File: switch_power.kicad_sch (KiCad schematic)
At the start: 32 parts

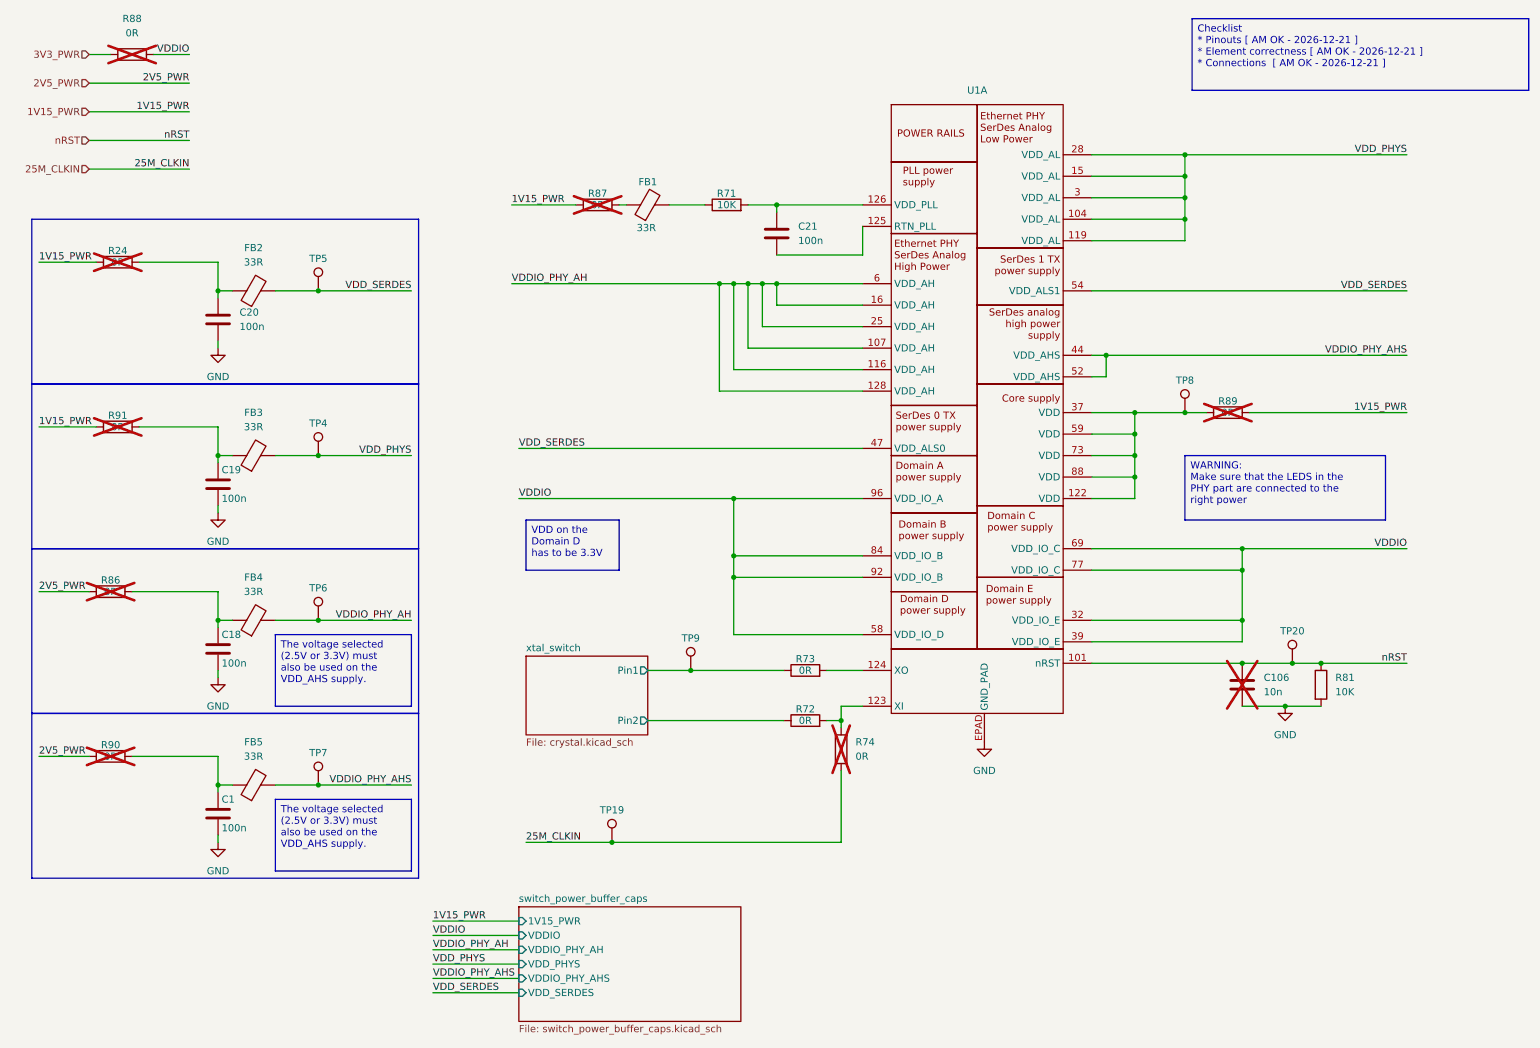
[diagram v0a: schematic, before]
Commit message: removes 25M CLK input for switch. Refs: #1
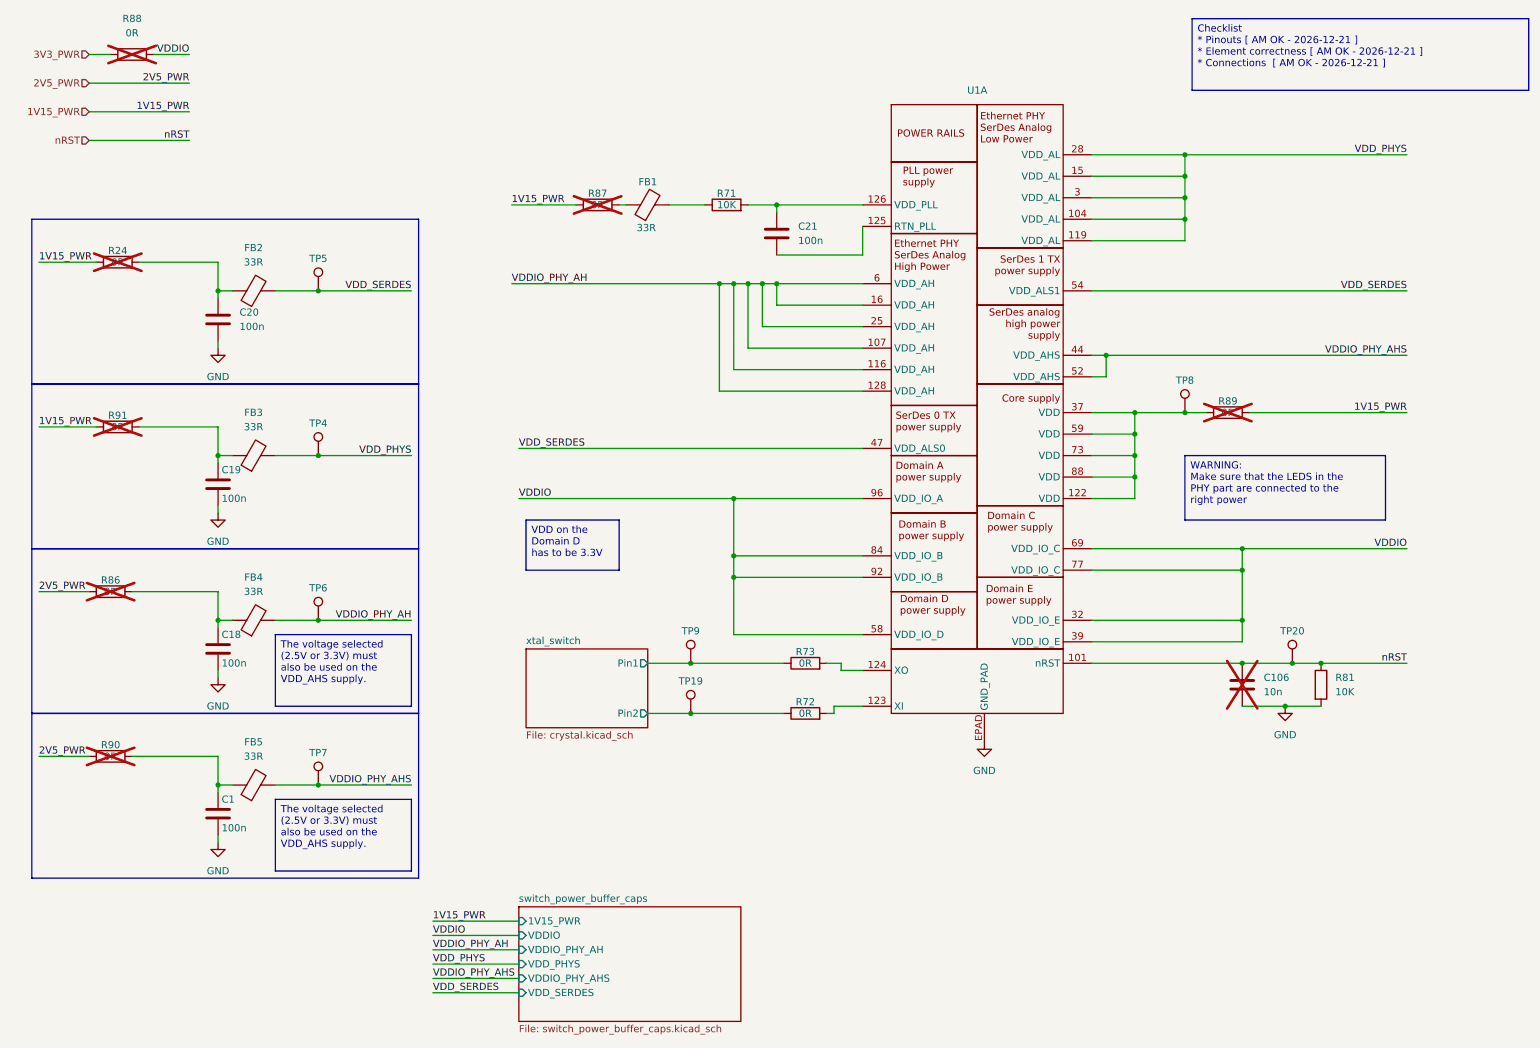
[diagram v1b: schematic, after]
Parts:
- removed R74: 0R, KL_Footprints:R_0603, symbol KL_R:R_0R_100mW_5_0603
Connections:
- net 25M_CLKIN is gone; now on net xtal_switch/Pin2: TP19.1
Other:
- moved on the sheet: R72, R73, TP9

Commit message: adds footprint for ferrite bead. Refs: #1
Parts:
- FB1, FB2, FB3, FB4, FB5: footprint (none) -> KL_Footprints:BLM18P; Digikey 490-5220-2-ND;490-5220-1-ND;490-5220-6-ND -> 490-5220-1-ND; Mouser 81-BLM18PG330SN1D -> 81-BLM18PG330SN1D
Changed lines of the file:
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@@
 			)
 		)
-		(property "Footprint" ""
-			(at 57.15 146.05 0)
+		(property "Footprint" "KL_Footprints:BLM18P"
+			(at 64.008 133.858 0)
 			(effects
 				(font
@@
 			)
 		)
-		(property "Datasheet" ""
-			(at 57.15 146.05 0)
+		(property "Datasheet" "https://pim.murata.com/asset/pim4/ferriteBeadInductortypefilter/ENFA0003_PDF_FERRITEBEADINDUCTORTYPEFILTER?lastModifiedDatetime=20250707190934"
+			(at 57.912 129.286 0)
 			(effects
 				(font
@@
 			)
 		)
-		(property "Mouser" " 81-BLM18PG330SN1D"
+		(property "Mouser" "81-BLM18PG330SN1D"
 			(at 39.37 147.574 0)
 			(effects
@@
 			)
 		)
-		(property "Digikey" "490-5220-2-ND;490-5220-1-ND;490-5220-6-ND"
+		(property "Digikey" "490-5220-1-ND"
 			(at 43.434 140.97 0)
 			(effects
@@
 			)
 		)
-		(property "Footprint" ""
-			(at 57.15 87.63 0)
+		(property "Footprint" "KL_Footprints:BLM18P"
+			(at 64.008 75.438 0)
 			(effects
 				(font
@@
 			)
 		)
-		(property "Datasheet" ""
-			(at 57.15 87.63 0)
+		(property "Datasheet" "https://pim.murata.com/asset/pim4/ferriteBeadInductortypefilter/ENFA0003_PDF_FERRITEBEADINDUCTORTYPEFILTER?lastModifiedDatetime=20250707190934"
+			(at 57.912 70.866 0)
 			(effects
 				(font
@@
 			)
 		)
-		(property "Mouser" " 81-BLM18PG330SN1D"
+		(property "Mouser" "81-BLM18PG330SN1D"
 			(at 39.37 89.154 0)
 			(effects
@@
 			)
 		)
-		(property "Digikey" "490-5220-2-ND;490-5220-1-ND;490-5220-6-ND"
+		(property "Digikey" "490-5220-1-ND"
 			(at 43.434 82.55 0)
 			(effects
@@
 			)
 		)
-		(property "Footprint" ""
-			(at 127 43.18 0)
+		(property "Footprint" "KL_Footprints:BLM18P"
+			(at 133.858 30.988 0)
 			(effects
 				(font
@@
 			)
 		)
-		(property "Datasheet" ""
-			(at 127 43.18 0)
+		(property "Datasheet" "https://pim.murata.com/asset/pim4/ferriteBeadInductortypefilter/ENFA0003_PDF_FERRITEBEADINDUCTORTYPEFILTER?lastModifiedDatetime=20250707190934"
+			(at 127.762 26.416 0)
 			(effects
 				(font
@@
 			)
 		)
-		(property "Mouser" " 81-BLM18PG330SN1D"
+		(property "Mouser" "81-BLM18PG330SN1D"
 			(at 109.22 44.704 0)
 			(effects
@@
 			)
 		)
-		(property "Digikey" "490-5220-2-ND;490-5220-1-ND;490-5220-6-ND"
+		(property "Digikey" "490-5220-1-ND"
 			(at 113.284 38.1 0)
 			(effects
@@
 			)
 		)
-		(property "Footprint" ""
-			(at 57.15 116.84 0)
+		(property "Footprint" "KL_Footprints:BLM18P"
+			(at 64.008 104.648 0)
 			(effects
 				(font
@@
 			)
 		)
-		(property "Datasheet" ""
-			(at 57.15 116.84 0)
+		(property "Datasheet" "https://pim.murata.com/asset/pim4/ferriteBeadInductortypefilter/ENFA0003_PDF_FERRITEBEADINDUCTORTYPEFILTER?lastModifiedDatetime=20250707190934"
+			(at 57.912 100.076 0)
 			(effects
 				(font
@@
 			)
 		)
-		(property "Mouser" " 81-BLM18PG330SN1D"
+		(property "Mouser" "81-BLM18PG330SN1D"
 			(at 39.37 118.364 0)
 			(effects
@@
 			)
 		)
-		(property "Digikey" "490-5220-2-ND;490-5220-1-ND;490-5220-6-ND"
+		(property "Digikey" "490-5220-1-ND"
 			(at 43.434 111.76 0)
 			(effects
@@
 			)
 		)
-		(property "Footprint" ""
-			(at 57.15 58.42 0)
+		(property "Footprint" "KL_Footprints:BLM18P"
+			(at 64.008 46.228 0)
 			(effects
 				(font
@@
 			)
 		)
-		(property "Datasheet" ""
-			(at 57.15 58.42 0)
+		(property "Datasheet" "https://pim.murata.com/asset/pim4/ferriteBeadInductortypefilter/ENFA0003_PDF_FERRITEBEADINDUCTORTYPEFILTER?lastModifiedDatetime=20250707190934"
+			(at 57.912 41.656 0)
 			(effects
 				(font
@@
 			)
 		)
-		(property "Mouser" " 81-BLM18PG330SN1D"
+		(property "Mouser" "81-BLM18PG330SN1D"
 			(at 39.37 59.944 0)
 			(effects
@@
 			)
 		)
-		(property "Digikey" "490-5220-2-ND;490-5220-1-ND;490-5220-6-ND"
+		(property "Digikey" "490-5220-1-ND"
 			(at 43.434 53.34 0)
 			(effects

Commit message: updates component details for ordering. Refs: #1
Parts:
- TP19, TP20, TP4, TP5, TP6, TP7, TP8, TP9: now left out of the parts list
- U1: value ~ -> LAN96455F-I/8MW; Digikey (none) -> 150-LAN96455F-I/8MW-ND; Mouser (none) -> 579-LAN96455FI8MW; manf# LAN96455F-I/8MW -> (none)

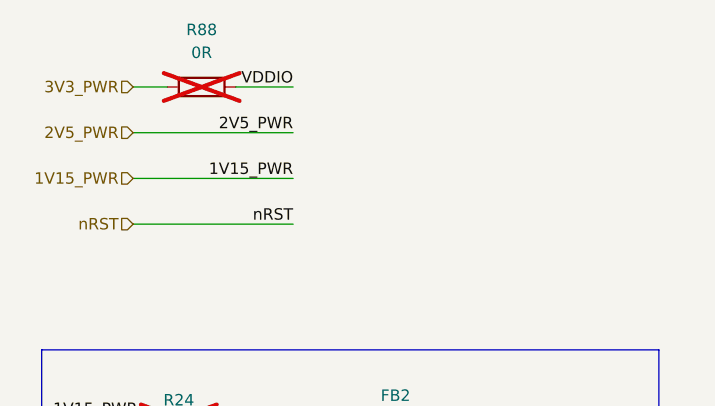
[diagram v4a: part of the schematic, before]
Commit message: moves 0R rail resistors for switch and controller to correct position. Refs: #1
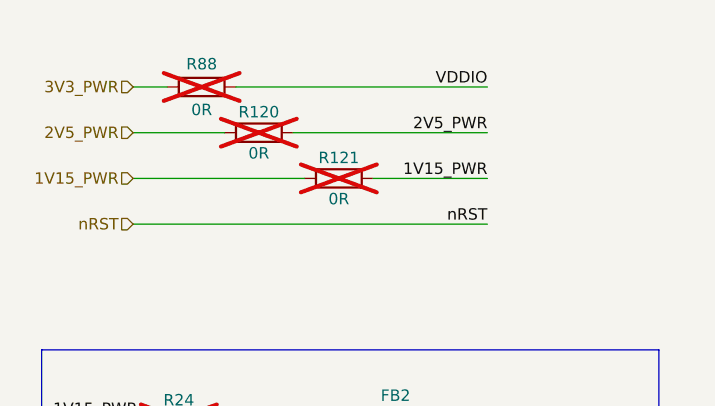
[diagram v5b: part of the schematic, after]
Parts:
- added R120, R121: 0R, KL_Footprints:R_2512, symbol KL_R:R_0R_2W_5_2512
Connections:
- net 1V15_PWR: now also R121.1, R121.2
- net 2V5_PWR: now also R120.1, R120.2

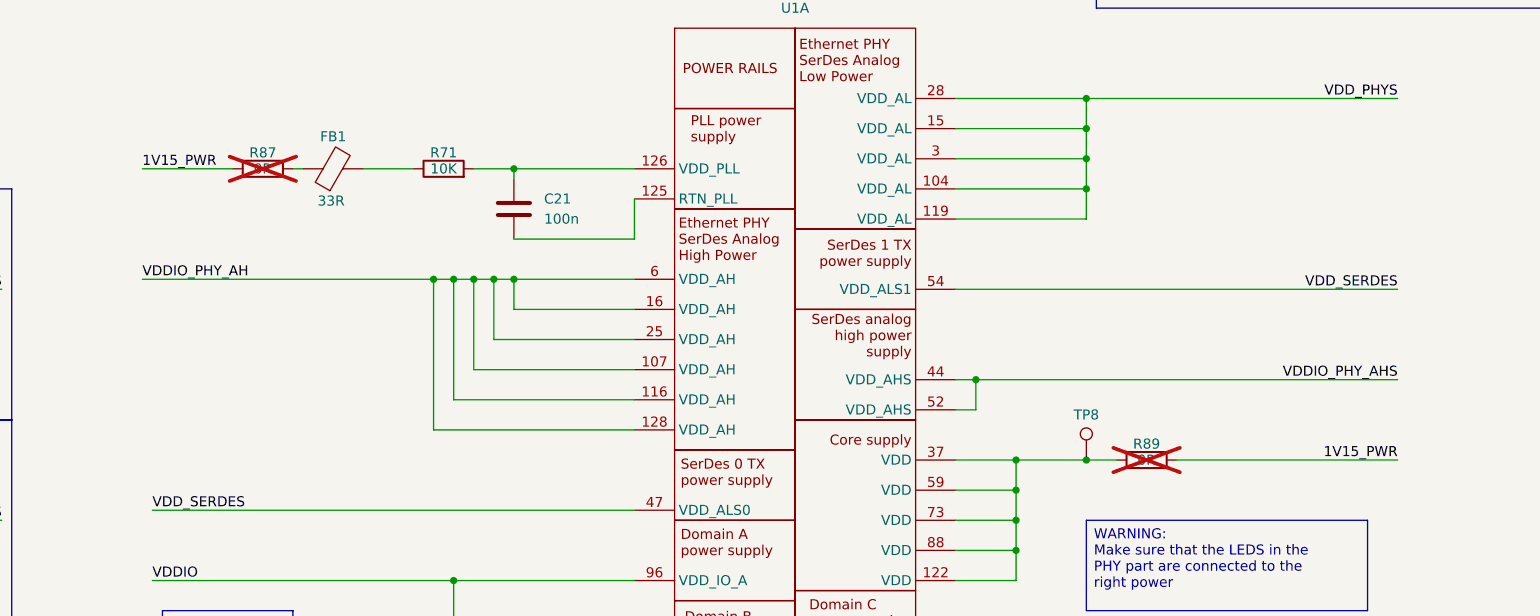
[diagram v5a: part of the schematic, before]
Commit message: moves overseen 0R rail resistors to the correct place. Refs: #1
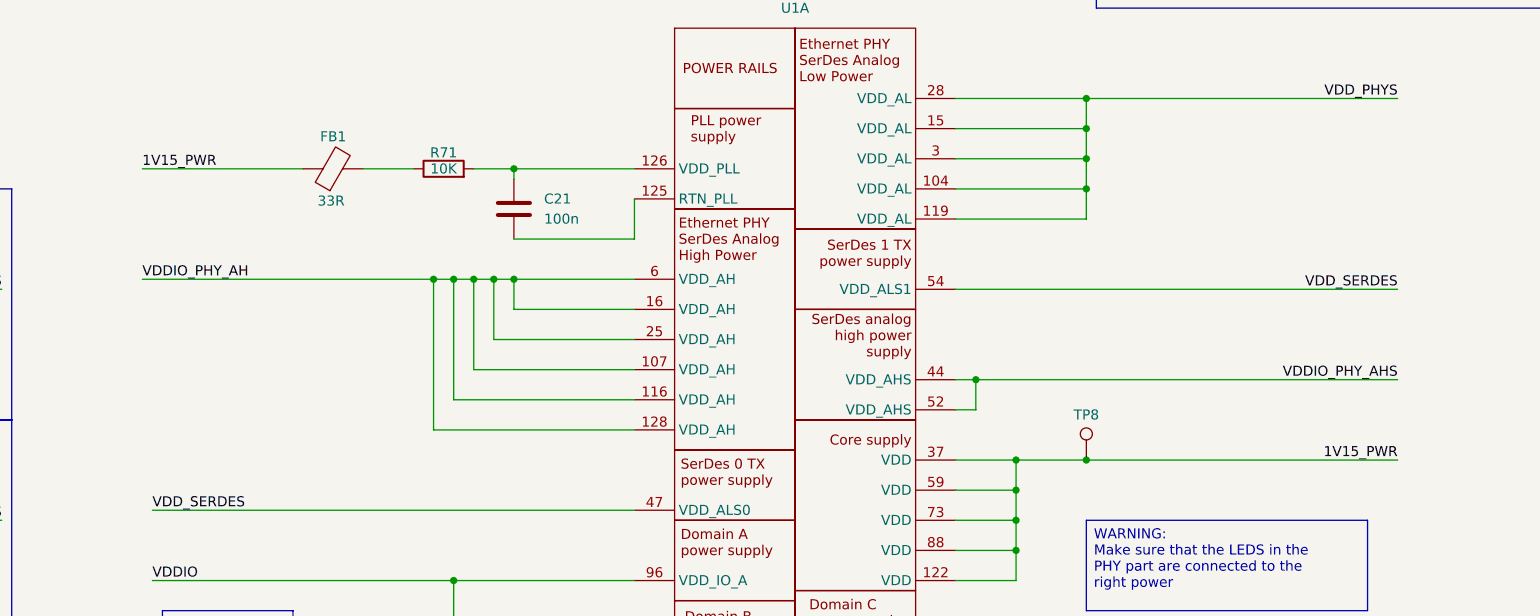
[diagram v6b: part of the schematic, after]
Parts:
- removed R87, R89: 0R, KL_Footprints:R_2512, symbol KL_R:R_0R_2W_5_2512
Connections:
- net 1V15_PWR: now also FB1.1, TP8.1, U1.122 (VDD), U1.37 (VDD), U1.59 (VDD), U1.73 (VDD), U1.88 (VDD)

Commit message: initial commit for automatic current consumption calculation. Refs: #9
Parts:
- U1: I_DD_1V15_max_A (none) -> 0.935; I_DD_AH25_2V5_max_A (none) -> 0.475; I_DD_AH33_3V3_max_A (none) -> 0.505; I_DD_ALSx_1V15_max_A (none) -> 0.025; I_DD_AL_1V15_max_A (none) -> 0.400; I_DD_IO25_2V5_max_A (none) -> 0.045; I_DD_IO33_3V3_max_A (none) -> 0.075; I_DD_IOD (none) -> 0.005
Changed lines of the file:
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@@
+			)
+		)
+		(property "I_DD_1V15_max_A" "0.935"
+			(at 170.18 49.53 0)
+			(effects
+				(font
+					(size 1.27 1.27)
+				)
+				(hide yes)
+			)
+		)
+		(property "I_DD_AL_1V15_max_A" "0.400"
+			(at 170.18 49.53 0)
+			(effects
+				(font
+					(size 1.27 1.27)
+				)
+				(hide yes)
+			)
+		)
+		(property "I_DD_ALSx_1V15_max_A" "0.025"
+			(at 170.18 49.53 0)
+			(effects
+				(font
+					(size 1.27 1.27)
+				)
+				(hide yes)
+			)
+		)
+		(property "I_DD_AH25_2V5_max_A" "0.475"
+			(at 170.18 49.53 0)
+			(effects
+				(font
+					(size 1.27 1.27)
+				)
+				(hide yes)
+			)
+		)
+		(property "I_DD_AH33_3V3_max_A" "0.505"
+			(at 170.18 49.53 0)
+			(effects
+				(font
+					(size 1.27 1.27)
+				)
+				(hide yes)
+			)
+		)
+		(property "I_DD_IO25_2V5_max_A" "0.045"
+			(at 170.18 49.53 0)
+			(effects
+				(font
+					(size 1.27 1.27)
+				)
+				(hide yes)
+			)
+		)
+		(property "I_DD_IO33_3V3_max_A" "0.075"
+			(at 170.18 49.53 0)
+			(effects
+				(font
+					(size 1.27 1.27)
+				)
+				(hide yes)
+			)
+		)
+		(property "I_DD_IOD" "0.005"
+			(at 170.18 49.53 0)
+			(effects
+				(font
+					(size 1.27 1.27)
+				)
+				(hide yes)
 			)
 		)
